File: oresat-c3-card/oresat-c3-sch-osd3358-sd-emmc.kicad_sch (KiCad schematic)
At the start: 41 parts, among them J5 DM3BT-DSF-PEJS, U1 OSD3358-1G-ISM, U8 TCAN330, U9 SFEM016GB1EA1TO-I-GE-121-STD

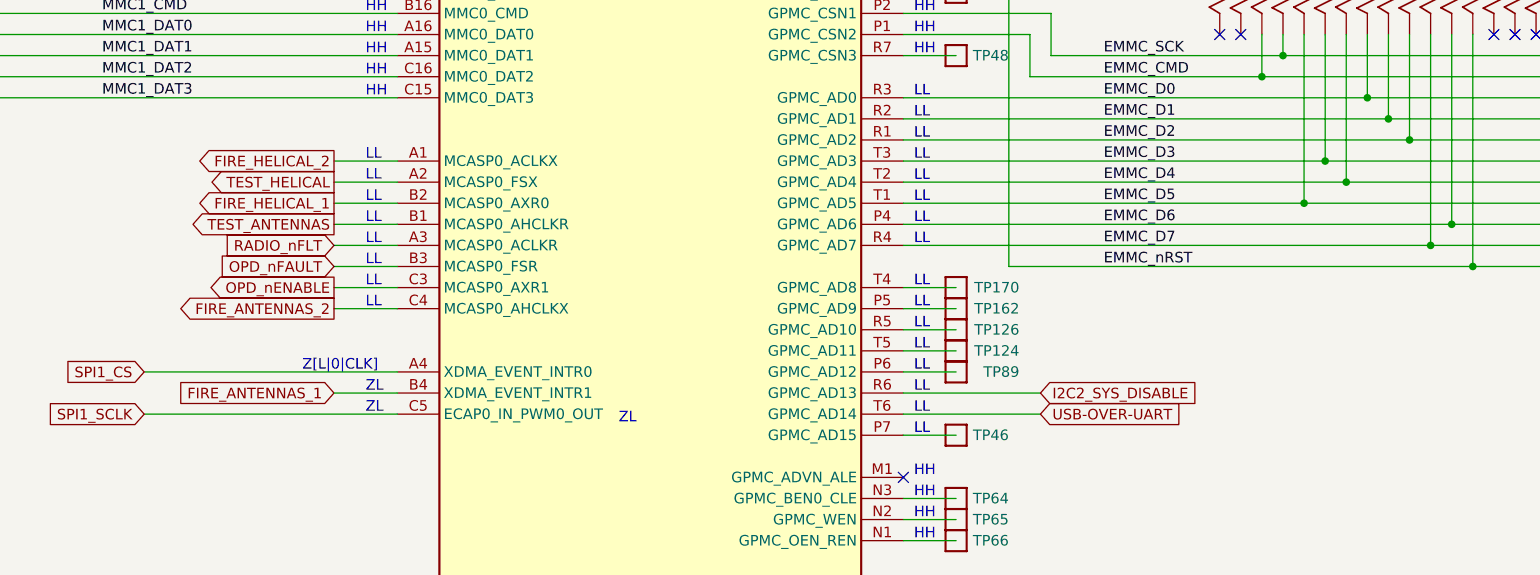
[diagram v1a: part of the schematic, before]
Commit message: schematic changes following design review
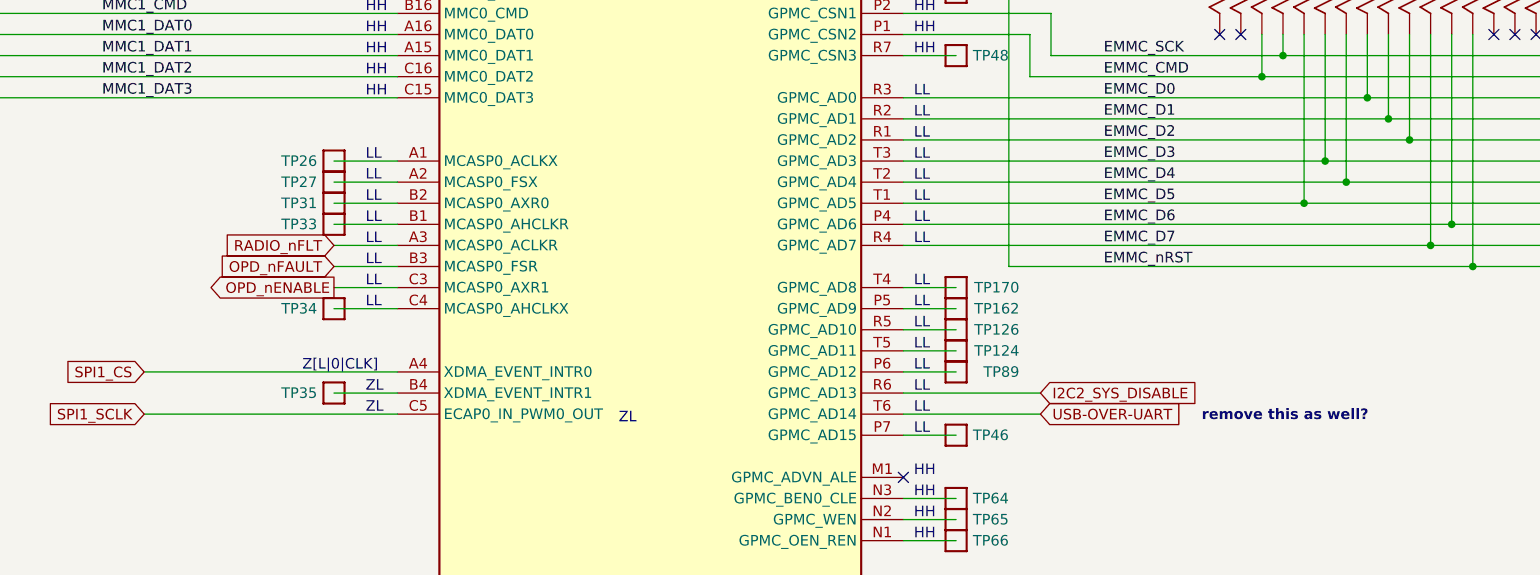
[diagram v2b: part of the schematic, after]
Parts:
- added TP26, TP27, TP31, TP33, TP34, TP35: Test-Point, oresat-misc:TestPoint_Pad_D1.0mm, symbol oresat-misc:Test-Point-1mm-round
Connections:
- net FIRE_ANTENNAS_1: no longer names the net of U1.B4 (XDMA_EVENT_INTR1)
- net FIRE_ANTENNAS_1: now also TP35.1
- net FIRE_ANTENNAS_2: no longer names the net of U1.C4 (MCASP0_AHCLKX)
- net FIRE_ANTENNAS_2: now also TP34.1
- net FIRE_HELICAL_1: no longer names the net of U1.B2 (MCASP0_AXR0)
- net FIRE_HELICAL_1: now also TP31.1
- net FIRE_HELICAL_2: no longer names the net of U1.A1 (MCASP0_ACLKX)
- net FIRE_HELICAL_2: now also TP26.1
- net TEST_ANTENNAS: no longer names the net of U1.B1 (MCASP0_AHCLKR)
- net TEST_ANTENNAS: now also TP33.1
- net TEST_HELICAL: no longer names the net of U1.A2 (MCASP0_FSX)
- net TEST_HELICAL: now also TP27.1
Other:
- note added: "remove this as well?"

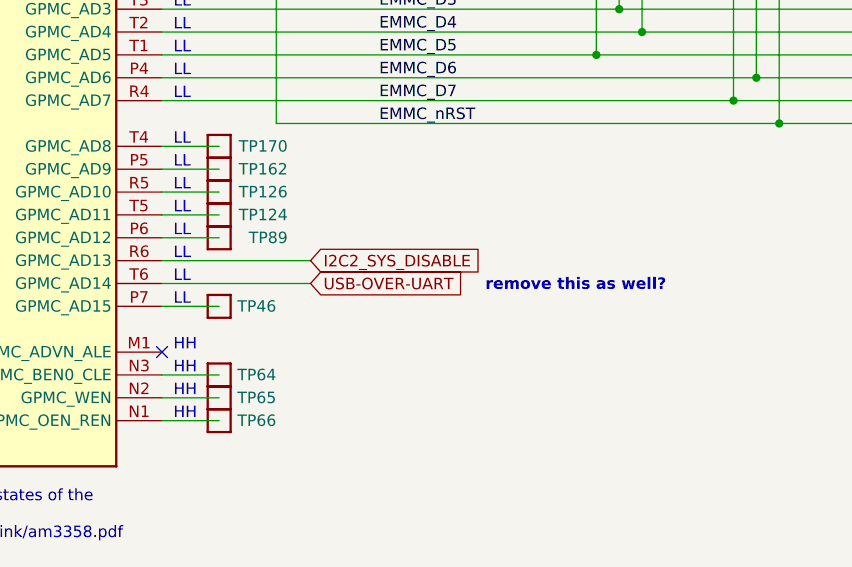
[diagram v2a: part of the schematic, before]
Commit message: Additional C3 design review changes and routing progress
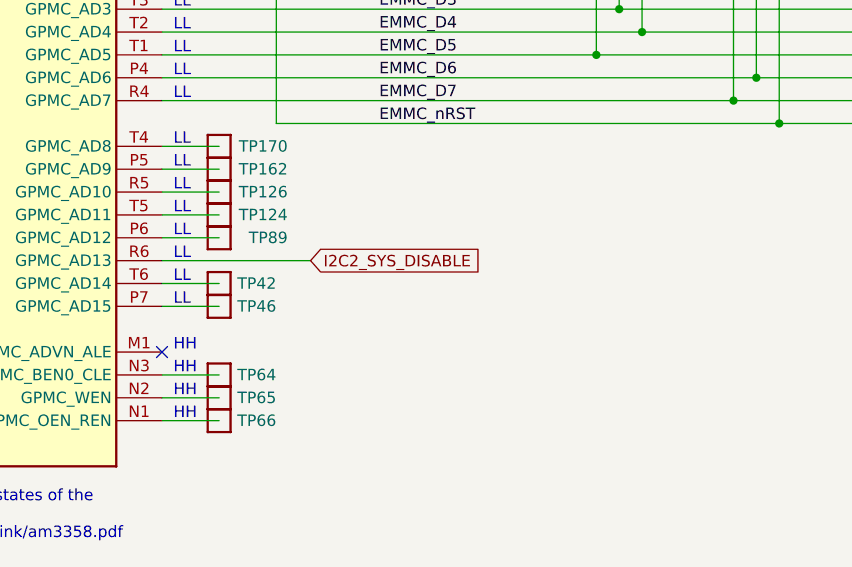
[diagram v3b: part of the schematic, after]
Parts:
- added TP42: Test-Point, oresat-misc:TestPoint_Pad_D1.0mm, symbol oresat-misc:Test-Point-1mm-round
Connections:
- net USB-OVER-UART: no longer names the net of U1.T6 (GPMC_AD14)
- net USB-OVER-UART: now also TP42.1
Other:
- note removed: "remove this as well?"
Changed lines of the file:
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@@
 		)
 	)
-	(text "remove this as well?"
-		(exclude_from_sim no)
-		(at 269.494 200.914 0)
-		(effects
-			(font
-				(size 1.27 1.27)
-				(thickness 0.254)
-				(bold yes)
-			)
-		)
-	)
 	(text "LL"
 		(exclude_from_sim no)
@@
 	(wire
 		(pts
-			(xy 223.52 200.66) (xy 240.03 200.66)
+			(xy 223.52 200.66) (xy 229.87 200.66)
 		)
 		(stroke
@@
 		)
 	)
-	(global_label "USB-OVER-UART"
-		(shape input)
-		(at 240.03 200.66 0)
-		(fields_autoplaced yes)
-		(effects
-			(font
-				(size 1.27 1.27)
-			)
-			(justify left)
-		)
-		(property "Intersheetrefs" "${INTERSHEET_REFS}"
-			(at 259.4648 200.66 0)
-			(effects
-				(font
-					(size 1.27 1.27)
-				)
-				(justify left)
-			)
-		)
-	)
 	(global_label "OPD_nFAULT"
 		(shape input)
@@
 					(unit 1)
 				)
+			)
+		)
+	)
+	(symbol
+		(lib_id "oresat-misc:Test-Point-1mm-round")
+		(at 229.87 200.66 90)
+		(unit 1)
+		(exclude_from_sim yes)
+		(in_bom no)
+		(on_board yes)
+		(dnp no)
+		(property "Reference" "TP42"
+			(at 236.22 200.66 90)
+			(effects
+				(font
+					(size 1.27 1.27)
+				)
+				(justify left)
+			)
+		)
+		(property "Value" "Test-Point"
+			(at 227.33 200.66 0)
+			(effects
+				(font
+					(size 1.27 1.27)
+				)
+				(hide yes)
+			)
+		)
+		(property "Footprint" "oresat-misc:TestPoint_Pad_D1.0mm"
+			(at 219.71 200.66 0)
+			(effects
+				(font
+					(size 1.27 1.27)
+				)
+				(hide yes)
+			)
+		)
+		(property "Datasheet" ""
+			(at 229.87 200.66 0)
+			(effects
+				(font
+					(size 1.27 1.27)
+				)
+				(hide yes)
+			)
+		)
+		(property "Description" "1mm round SMT test point"
+			(at 229.87 200.66 0)
+			(effects
+				(font
+					(size 1.27 1.27)
+				)
+				(hide yes)
+			)
+		)
+		(pin "1"
+		)
+		(instances
+			(project "oresat-c3"
+				(path "/65d12cdd-c326-4033-9053-c59fa4e0b25e/f3d147ad-4cea-4d77-ae60-95882b03454e"
+					(reference "TP42")
+					(unit 1)
+				)

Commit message: completed rough rounting on left side and l band rf side
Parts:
- J5: footprint oresat-footprints:J-Hirose-DM3BT-DSF-PEJS -> oresat-connectors:J-Hirose-DM3BT-DSF-PEJS
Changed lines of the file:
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@@
 			)
 		)
-		(property "Description" "Blue 470nm LED Indication - Discrete 3.2V 0603 (1608 Metric)"
+		(property "Description" "Light emitting diode, small symbol"
 			(at 293.37 104.14 0)
 			(effects
@@
 			)
 		)
+		(property "Sim.Pin" "1=K 2=A"
+			(at 293.37 104.14 0)
+			(effects
+				(font
+					(size 1.27 1.27)
+				)
+				(hide yes)
+			)
+		)
 		(pin "1"
 		)
@@
 			)
 		)
-		(property "Description" "Blue 470nm LED Indication - Discrete 3.2V 0603 (1608 Metric)"
+		(property "Description" "Light emitting diode, small symbol"
 			(at 293.37 111.76 0)
 			(effects
@@
 			)
 		)
+		(property "Sim.Pin" "1=K 2=A"
+			(at 293.37 111.76 0)
+			(effects
+				(font
+					(size 1.27 1.27)
+				)
+				(hide yes)
+			)
+		)
 		(pin "1"
 		)
@@
 			)
 		)
-		(property "Description" "Blue 470nm LED Indication - Discrete 3.2V 0603 (1608 Metric)"
+		(property "Description" "Light emitting diode, small symbol"
 			(at 293.37 119.38 0)
 			(effects
@@
 			)
 		)
+		(property "Sim.Pin" "1=K 2=A"
+			(at 293.37 119.38 0)
+			(effects
+				(font
+					(size 1.27 1.27)
+				)
+				(hide yes)
+			)
+		)
 		(pin "1"
 		)
@@
 			)
 		)
-		(property "Footprint" "oresat-footprints:J-Hirose-DM3BT-DSF-PEJS"
+		(property "Footprint" "oresat-connectors:J-Hirose-DM3BT-DSF-PEJS"
 			(at 58.42 137.16 0)
 			(effects
@@
 			)
 		)
-		(property "Description" "Blue 470nm LED Indication - Discrete 3.2V 0603 (1608 Metric)"
+		(property "Description" "Light emitting diode, small symbol"
 			(at 293.37 127 0)
 			(effects
@@
 			(at 293.37 127 0)
 			(effects
+				(font
+					(size 1.27 1.27)
+				)
+				(hide yes)
+			)
+		)
+		(property "Sim.Pin" "1=K 2=A"
+			(at 293.37 127 0)
+			(effects

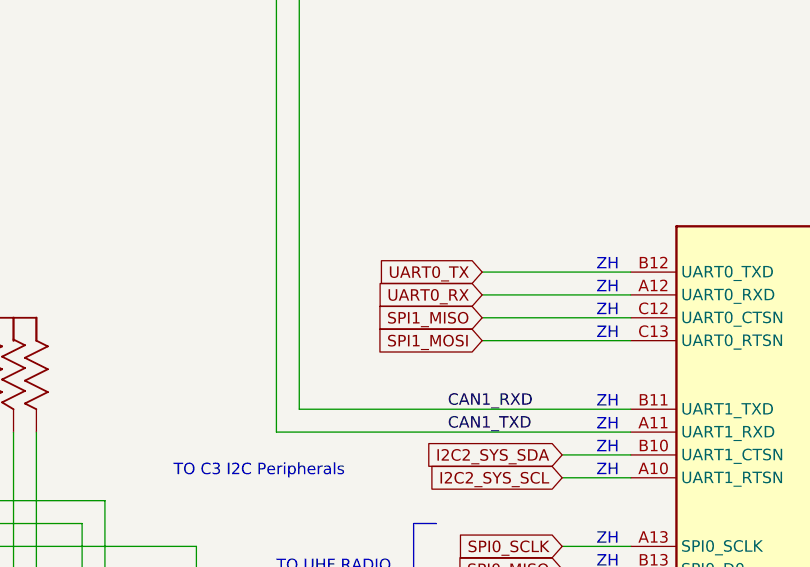
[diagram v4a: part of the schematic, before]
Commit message: finished connecting and routing, starting on clean up
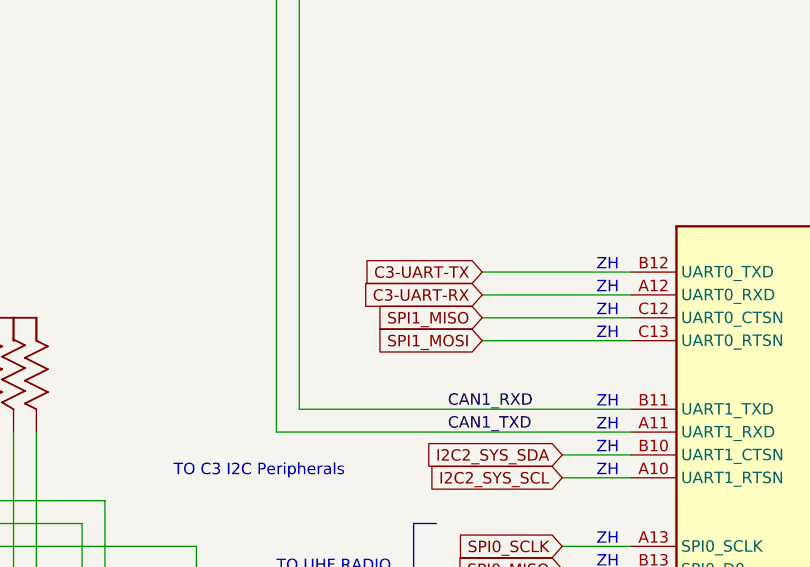
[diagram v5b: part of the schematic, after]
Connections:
- net UART0_RX renamed C3-UART-RX
- net UART0_TX renamed C3-UART-TX
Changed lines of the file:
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@@
+		)
+	)
+	(global_label "C3-UART-RX"
+		(shape input)
+		(at 146.05 104.14 180)
+		(effects
+			(font
+				(size 1.27 1.27)
+			)
+			(justify right)
+		)
+		(property "Intersheetrefs" "${INTERSHEET_REFS}"
+			(at 132.08 104.14 0)
+			(effects
+				(font
+					(size 1.27 1.27)
+				)
+				(justify right)
+			)
 		)
 	)
@@
 		)
 	)
-	(global_label "UART0_RX"
-		(shape input)
-		(at 146.05 104.14 180)
-		(fields_autoplaced yes)
-		(effects
-			(font
-				(size 1.27 1.27)
-			)
-			(justify right)
-		)
-		(property "Intersheetrefs" "${INTERSHEET_REFS}"
-			(at 133.8309 104.14 0)
-			(effects
-				(font
-					(size 1.27 1.27)
-				)
-				(justify right)
-			)
-		)
-	)
 	(global_label "SPI0_CS"
 		(shape input)
@@
 		(property "Intersheetrefs" "${INTERSHEET_REFS}"
 			(at 144.2933 139.7 0)
+			(effects
+				(font
+					(size 1.27 1.27)
+				)
+				(justify right)
+			)
+		)
+	)
+	(global_label "C3-UART-TX"
+		(shape input)
+		(at 146.05 101.6 180)
+		(effects
+			(font
+				(size 1.27 1.27)
+			)
+			(justify right)
+		)
+		(property "Intersheetrefs" "${INTERSHEET_REFS}"
+			(at 131.826 101.6 0)
 			(effects
 				(font
@@
 			(effects
 				(font
-					(size 1.27 1.27)
-				)
-				(justify right)
-			)
-		)
-	)
-	(global_label "UART0_TX"
-		(shape input)
-		(at 146.05 101.6 180)
-		(fields_autoplaced yes)
-		(effects
-			(font
-				(size 1.27 1.27)
-			)
-			(justify right)
-		)
-		(property "Intersheetrefs" "${INTERSHEET_REFS}"
-			(at 134.1333 101.6 0)
-			(effects
-				(font

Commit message: Design review on power and RF
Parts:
- U1: Distributor (none) -> DigiKey; MPN OSD3358-1G-ISM -> OSD3358-512M-BSM
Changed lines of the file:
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@@
 			)
 		)
+		(property "Sim.Pins" "1=K 2=A"
+			(at 293.37 104.14 0)
+			(effects
+				(font
+					(size 1.27 1.27)
+				)
+				(hide yes)
+			)
+		)
 		(pin "1"
 		)
@@
 			)
 		)
-		(property "Description" "eMMC 16GB E-MMC MLC EM-20 IND"
+		(property "Description" "IC FLASH 16GBIT EMMC 153FBGA"
 			(at 330.2 175.26 0)
 			(effects
@@
 		(pin "E9"
 		)
-		(pin "E9"
-		)
 		(pin "F1"
 		)
@@
 			)
 		)
+		(property "Sim.Pins" "1=K 2=A"
+			(at 293.37 111.76 0)
+			(effects
+				(font
+					(size 1.27 1.27)
+				)
+				(hide yes)
+			)
+		)
 		(pin "1"
 		)
@@
 			)
 		)
-		(property "Description" "Embedded Module ARM® Cortex®-A8, AM3358 1GHz 1GB"
+		(property "Description" "OSD335x Embedded Module 1GHz 512MB"
 			(at 193.04 53.34 0)
 			(effects
@@
 			)
 		)
-		(property "MPN" "OSD3358-1G-ISM"
+		(property "MPN" "OSD3358-512M-BSM"
 			(at 193.04 58.42 0)
 			(effects
@@
 			)
 		)
+		(property "Distributor" "DigiKey"
+			(at 193.04 55.88 0)
+			(effects
+				(font
+					(size 1.27 1.27)
+				)
+				(hide yes)
+			)
+		)
 		(pin "C10"
 		)
@@
 			)
 		)
+		(property "Sim.Pins" "1=K 2=A"
+			(at 293.37 119.38 0)
+			(effects
+				(font
+					(size 1.27 1.27)
+				)
+				(hide yes)
+			)
+		)
 		(pin "1"
 		)
@@
 			(at 293.37 127 0)
 			(effects
+				(font
+					(size 1.27 1.27)
+				)
+				(hide yes)
+			)
+		)
+		(property "Sim.Pins" "1=K 2=A"
+			(at 293.37 127 0)
+			(effects
